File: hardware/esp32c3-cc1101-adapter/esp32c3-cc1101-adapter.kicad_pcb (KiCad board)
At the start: 2 copper layers, 24 x 38 mm, 3 parts, among them J1 Conn_01x08, J2 Conn_01x08, J3 E07-M1101D

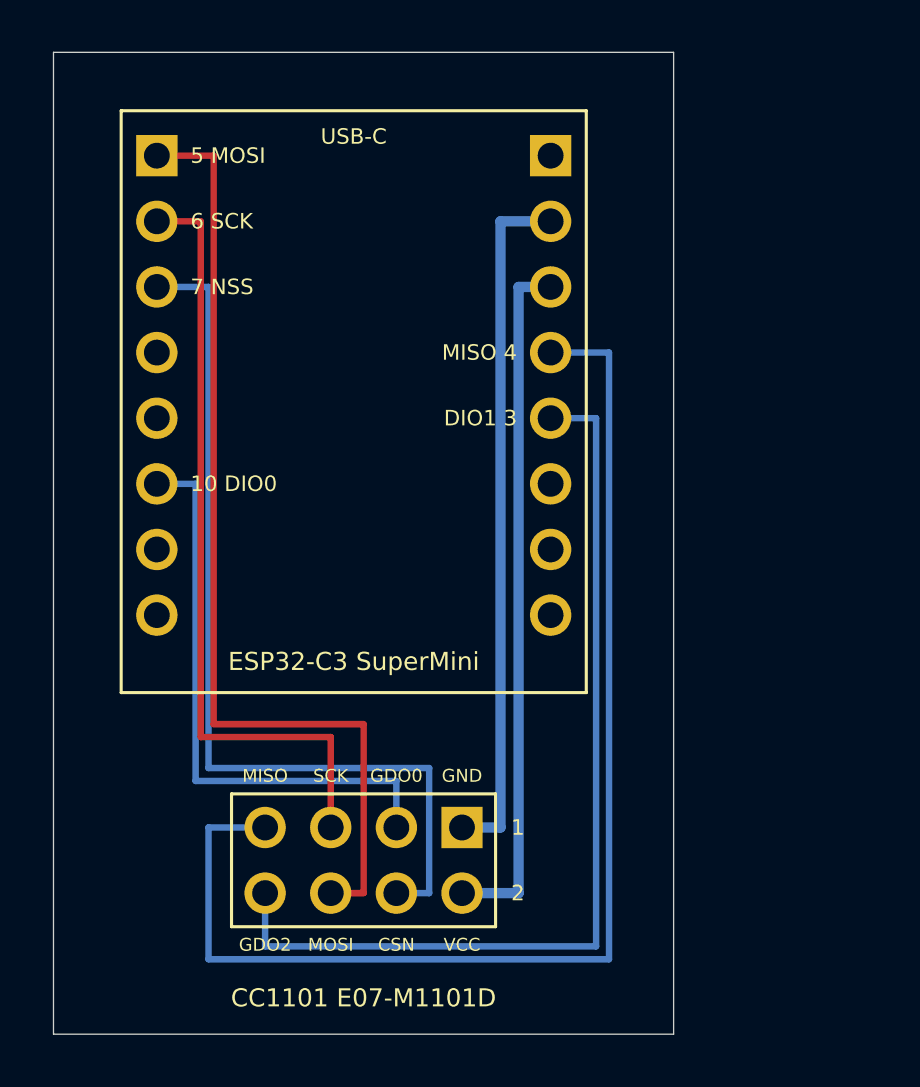
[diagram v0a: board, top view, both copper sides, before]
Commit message: Make the CC1101 adapter single-sided; add ESP32 pin names to silk
All tracks of the ESP32-C3 to CC1101 adapter now run on B.Cu (the
front keeps only the through-hole pad rings).  To make the eight nets
planar without jumpers the SuperMini lies on its side with USB-C off
the left edge, so its GPIO row sits above the socket and its power row
behind it; MISO and GDO2 go over the top of the power row and down the
left edge.  Board is 30 x 38 mm.

Both adapters now print the SuperMini's own pin names on the outer
side of each header row and the radio signal names on the inner side.
Layout plots now include B.Cu.

Co-Authored-By: Claude Fable 5.1 <noreply@anthropic.com>
Claude-Session: https://claude.ai/code/session_01JoGdh4Cg3VtTTDZi4gQuiN
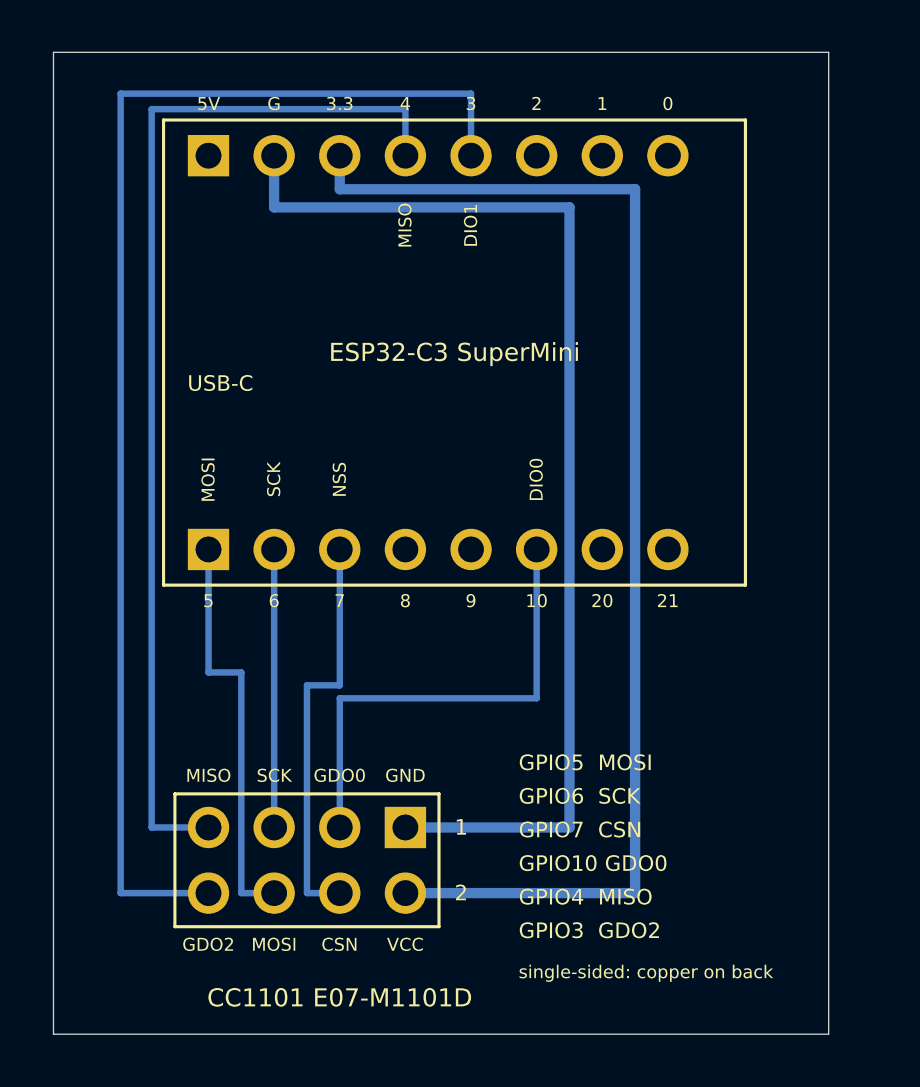
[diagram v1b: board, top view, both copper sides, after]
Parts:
- J1, J2: footprint Adapter:SuperMini_Header_1x08_P2.54mm_THT -> Adapter:SuperMini_Header_1x08_P2.54mm_THT_Row
- moved J1 15.4 mm to (106.0, 119.2)
- moved J2 13.2 mm to (106.0, 104.0)
- moved J3 2.19 mm to (113.6, 130.0)
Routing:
- net +3V3: track 26.9 -> 48.9 mm
- net MOSI: track 37.8 -> 15.8 mm
- net NSS: track 35.3 -> 15.8 mm
- net SCK: track 30.2 -> 10.8 mm
- net GND: track 26.9 -> 43.8 mm
- net DIO1: track 37.1 -> 50.3 mm
- net MISO: track 48.5 -> 41.6 mm
- net DIO0: track 22.6 -> 18.4 mm
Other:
- board size 24 x 38 mm -> 30 x 38 mm
- board text added: "0"
- board text added: "10"
- board text added: "20"
- board text added: "21"
- board text added: "3"
- board text added: "3.3"
- board text added: "4"
- board text added: "5"
- board text added: "5V"
- board text added: "6"
- board text added: "7"
- board text added: "8"
- board text added: "9"
- board text added: "DIO0"
- board text added: "DIO1"
- board text added: "G"
- board text added: "GPIO10 GDO0"
- board text added: "GPIO3 GDO2"
- board text added: "GPIO4 MISO"
- board text added: "GPIO5 MOSI"
- board text added: "GPIO6 SCK"
- board text added: "GPIO7 CSN"
- board text added: "NSS"
- board text added: "single-sided: copper on back"
- board text removed: "10 DIO0"
- board text removed: "5 MOSI"
- board text removed: "6 SCK"
- board text removed: "7 NSS"
- board text removed: "DIO1 3"
- board text removed: "MISO 4"

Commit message: Rework the CC1101 adapter: castellated keyhole pads, corner holes, two-sided silk
* SuperMini pins land on keyhole pads (1.0 mm hole plus 1.6 x 3.4 mm oval
  copper reaching 1.2 mm past the SuperMini edge) so the module can be
  fitted with header pins or soldered flat by its castellations.
* The SuperMini body now overhangs the left edge by 0.5 mm so the USB-C
  connector hangs clear of the board.
* Four M2 mounting holes 2.4 mm in from the corners; the socket moves right
  so the plugged-in E07 board clears the bottom-left screw.
* Silkscreen on both sides (back copy mirrored), signal names next to the
  SuperMini use the CC1101's names (GDO0, GDO2, CSN).
* Board is 27 x 36.5 mm; all tracks stay on B.Cu.  MISO and GDO2 now run
  over the top of the power row, down the right of the SuperMini and under
  the socket.
* kicadgen: gr_line helper.

Co-Authored-By: Claude Fable 5.1 <noreply@anthropic.com>
Claude-Session: https://claude.ai/code/session_01JoGdh4Cg3VtTTDZi4gQuiN
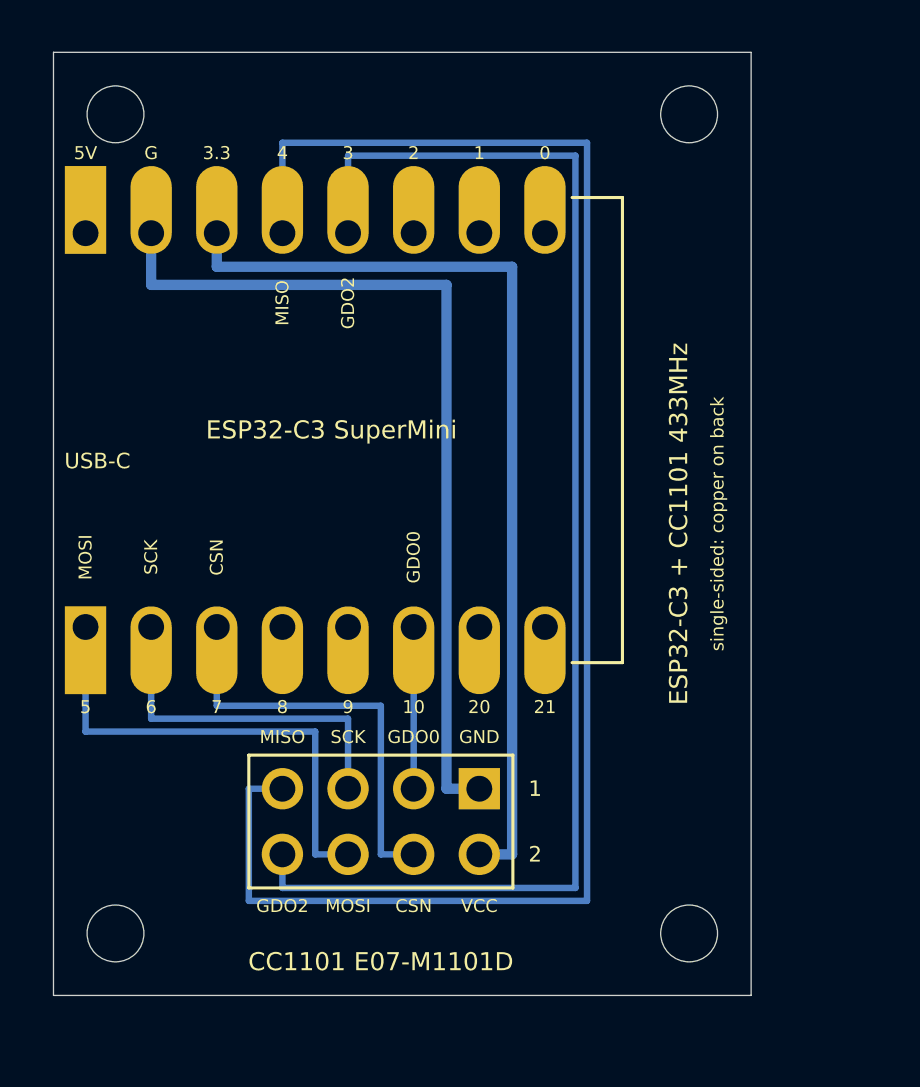
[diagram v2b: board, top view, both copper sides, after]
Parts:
- added H1: MountingHole, Adapter:MountingHole_2.2mm_M2, F.Cu at (102.4, 102.4)
- added H2: MountingHole, Adapter:MountingHole_2.2mm_M2, F.Cu at (124.6, 102.4)
- added H3: MountingHole, Adapter:MountingHole_2.2mm_M2, F.Cu at (102.4, 134.1)
- added H4: MountingHole, Adapter:MountingHole_2.2mm_M2, F.Cu at (124.6, 134.1)
- J1: footprint Adapter:SuperMini_Header_1x08_P2.54mm_THT_Row -> Adapter:SuperMini_Row_1x08_P2.54mm_THT_Castellated_Down
- J2: footprint Adapter:SuperMini_Header_1x08_P2.54mm_THT_Row -> Adapter:SuperMini_Row_1x08_P2.54mm_THT_Castellated_Up
- moved J1 5.63 mm to (101.2, 122.2)
- moved J2 5.63 mm to (101.2, 107.0)
- moved J3 3.23 mm to (116.5, 128.5)
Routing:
- net MISO: track 41.6 -> 63.4 mm
- net DIO0: track 18.4 -> 6.26 mm
- net +3V3: track 48.9 -> 36.7 mm
- net GND: track 43.8 -> 34.2 mm
- net SCK: track 10.8 -> 13.9 mm
- net MOSI: track 15.8 -> 19.0 mm
- net DIO1: track 50.3 -> 52.8 mm
- net NSS: track 15.8 -> 16.4 mm
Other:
- board size 30 x 38 mm -> 27 x 36.5 mm
- board text added: "ESP32-C3 + CC1101 433MHz"
- board text added: "single-sided: copper this side"
- board text removed: "DIO0"
- board text removed: "DIO1"
- board text removed: "GPIO10 GDO0"
- board text removed: "GPIO3 GDO2"
- board text removed: "GPIO4 MISO"
- board text removed: "GPIO5 MOSI"
- board text removed: "GPIO6 SCK"
- board text removed: "GPIO7 CSN"
- board text removed: "NSS"

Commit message: CC1101 adapter GND pour with antenna keepout; optional SMA on the SX1278 adapter
* kicadgen: Zone (copper pour / keepout) support, board revision "0" in
  every title block, KICAD_SHARE overridable for non-snap installs.
* scripts/fill_zones.py: fills zones with KiCad's own filler (pcbnew python,
  re-executed inside the snap when needed) and splices only the fill
  polygons into the generated file, so generation stays reproducible.
* CC1101 adapter: GND pour on F.Cu (all tracks remain on B.Cu), keepout on
  both layers under the SuperMini's ceramic antenna; MISO/GDO2 now run
  outside the SuperMini body instead of under its antenna.
* SX1278 adapter: 24 x 58 mm, optional edge-mount SMA jack (J4) on the
  bottom edge fed from the wire-hole antenna trace, ground legs on B.Cu
  with vias to the front pads.

Co-Authored-By: Claude Fable 5.1 <noreply@anthropic.com>
Claude-Session: https://claude.ai/code/session_01JoGdh4Cg3VtTTDZi4gQuiN
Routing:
- net MISO: track 63.4 -> 68.0 mm
- net DIO1: track 52.8 -> 57.4 mm
- added copper zone on F.Cu, net GND
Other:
- board text added: "all tracks on back; GND pour on front"
- board text added: "all tracks this side"
- board text removed: "single-sided: copper on back"
- board text removed: "single-sided: copper this side"
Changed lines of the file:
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@@
 	(paper "A4")
 	(title_block
-		(title "ESP32-C3 SuperMini to CC1101 E07-M1101D adapter (single-sided)")
-		(rev "1")
-		(comment 1 "Single-sided carrier joining an ESP32-C3 SuperMini to an Ebyte E07-M1101D-SMA CC1101 433MHz board via a 2x4 socket")
+		(title "ESP32-C3 SuperMini to CC1101 E07-M1101D adapter")
+		(rev "0")
+		(comment 1 "Carrier joining an ESP32-C3 SuperMini to an Ebyte E07-M1101D-SMA CC1101 433MHz board via a 2x4 socket; all tracks on the back, GND pour on the front")
 	)
 	(layers
@@
 		)
 	)
-	(gr_text "single-sided: copper on back"
+	(gr_text "all tracks on back; GND pour on front"
 		(at 125.7 118.25 90)
 		(layer "F.SilkS")
@@
 		)
 	)
-	(gr_text "single-sided: copper this side"
+	(gr_text "all tracks this side"
 		(at 125.7 118.25 270)
 		(layer "B.SilkS")
@@
 	(segment
 		(start 111.4 104)
-		(end 120.2 104)
+		(end 122.52 104)
 		(width 0.25)
 		(layer "B.Cu")
@@
 	)
 	(segment
-		(start 120.2 104)
-		(end 120.2 132.34)
+		(start 122.52 104)
+		(end 122.52 132.34)
 		(width 0.25)
 		(layer "B.Cu")
@@
 	)
 	(segment
-		(start 120.2 132.34)
+		(start 122.52 132.34)
 		(end 108.86 132.34)
 		(width 0.25)
@@
 	(segment
 		(start 108.86 103.5)
-		(end 120.65 103.5)
+		(end 122.97 103.5)
 		(width 0.25)
 		(layer "B.Cu")
@@
 	)
 	(segment
-		(start 120.65 103.5)
-		(end 120.65 132.84)
+		(start 122.97 103.5)
+		(end 122.97 132.84)
 		(width 0.25)
 		(layer "B.Cu")
@@
 	)
 	(segment
-		(start 120.65 132.84)
+		(start 122.97 132.84)
 		(end 107.56 132.84)
 		(width 0.25)
@@
 		(net 12)
 	)
+	(zone
+		(net 0)
+		(net_name "")
+		(layers "F.Cu" "B.Cu")
+		(name "antenna_keepout")
+		(hatch edge 0.5)
+		(connect_pads
+			(clearance 0)
+		)
+		(min_thickness 0.25)
+		(filled_areas_thickness no)
+		(keepout
+			(tracks not_allowed)
+			(vias not_allowed)
+			(pads allowed)
+			(copperpour not_allowed)
+			(footprints allowed)
+		)
+		(fill
+			(thermal_gap 0.5)
+			(thermal_bridge_width 0.5)
+		)
+		(polygon
+			(pts
+				(xy 118.22 108.3)
+				(xy 122.12 108.3)
+				(xy 122.12 120.94)
+				(xy 118.22 120.94)
+			)
+		)
+	)
+	(zone
+		(net 10)
+		(net_name "GND")
+		(layer "F.Cu")
+		(name "gnd_pour")
+		(hatch edge 0.5)
+		(connect_pads
+			(clearance 0.3)
+		)
+		(min_thickness 0.25)
+		(filled_areas_thickness no)
+		(fill yes
+			(thermal_gap 0.5)
+			(thermal_bridge_width 0.5)
+		)
+		(polygon
+			(pts
+				(xy 100.3 100.3)
+				(xy 126.7 100.3)
+				(xy 126.7 136.2)
+				(xy 100.3 136.2)
+			)
+		)
+	)
 	(embedded_fonts no)
